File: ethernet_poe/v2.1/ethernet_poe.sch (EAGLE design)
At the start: 81 parts, among them J3 ARJM11C7-104-AB-EW2, U1 AZ1117EH-3.3TRG1, U2 IFX91041, U3 W5500, U4 TPS26600PWPR, X1 25MHz

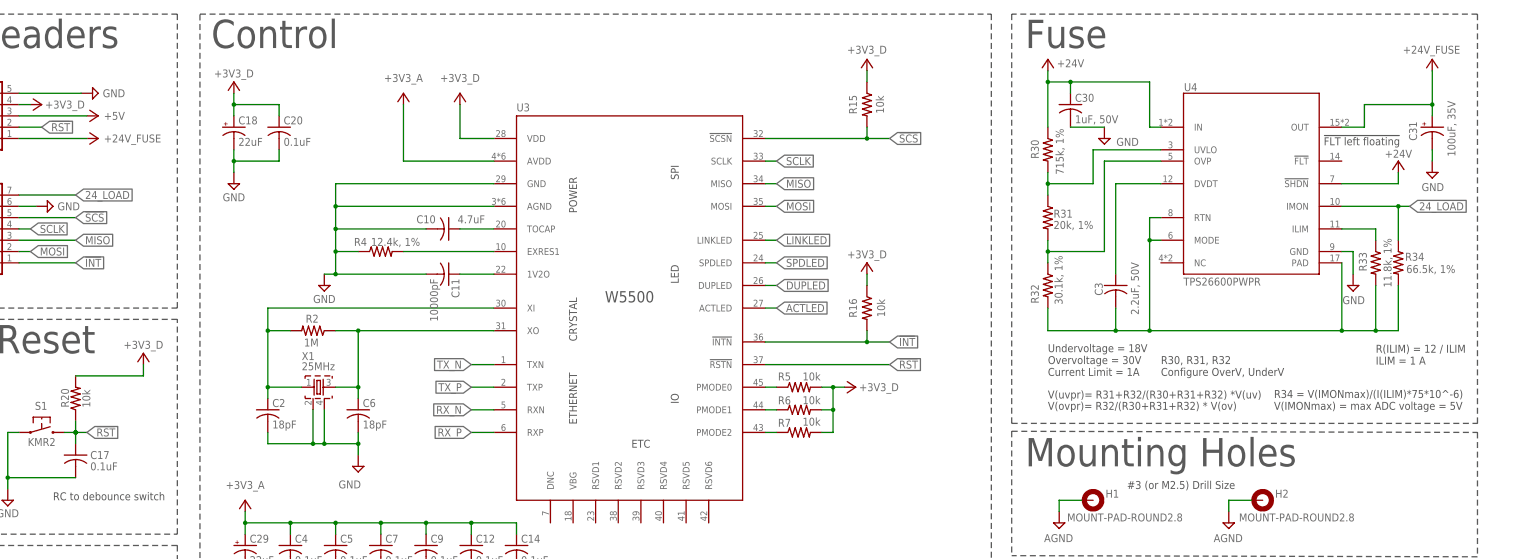
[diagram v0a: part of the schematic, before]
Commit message: Finished schematic and library changes
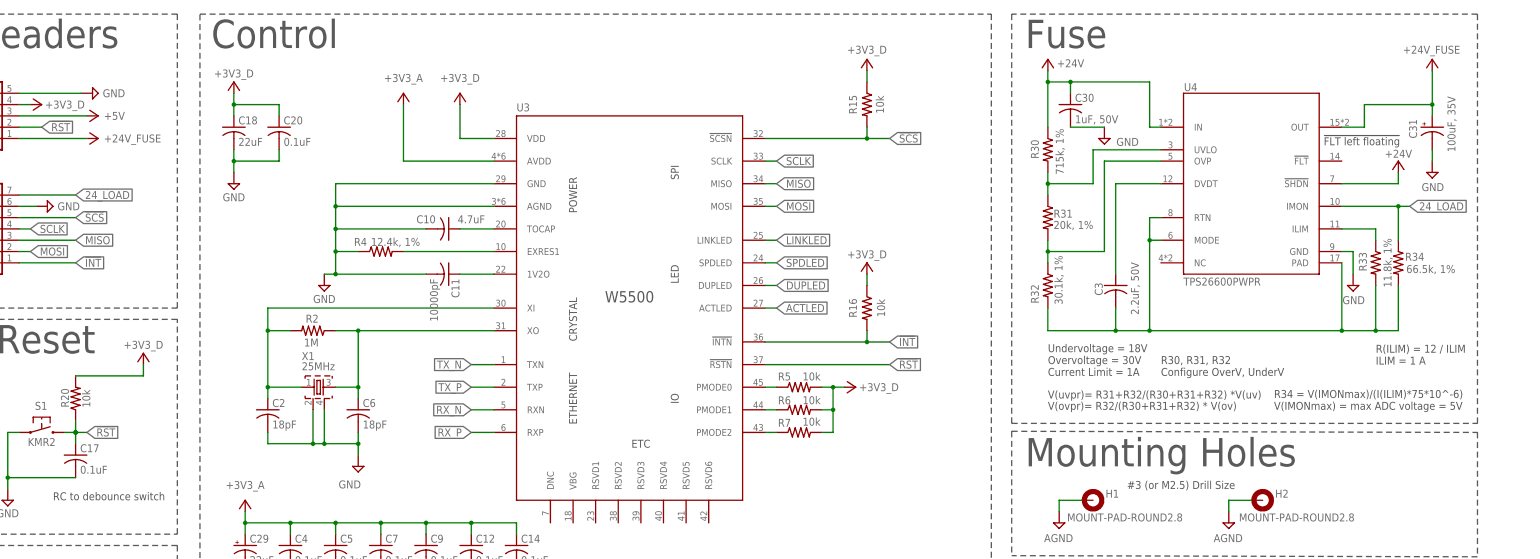
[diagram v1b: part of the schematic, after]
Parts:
- C15: DKPN (none) -> 732-8598-1-ND
- C17, C20, C21: device rcl:C-USC0603 -> adafruit:C-USC0402
- C18: device rcl:CPOL-USE2-5 -> rcl:C-USC0603
- C31: device rcl:CPOL-USE2-5 -> rcl:CPOL-USE2.5-7; DKPN (none) -> 732-8942-1-ND
- X1: device ethernet_poe:ABM10-25.000MHZ-18-E30-T3 -> ethernet_poe_v2.1:ABM10W-25.0000MHZ-6-K1Z-T3
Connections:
- net +3V3_D: now also C18.1; no longer C18.+
- net GND: now also C18.2; no longer C18.-

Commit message: Finished board changes
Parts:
- C1: value 22nF, 50V -> 0.022uF, 50V
- L1: device Wurth_Electronic_Inductors:WE-PD_7345_744777147 -> ethernet_poe_v2.1:7447709470_7447709470
- renumbered D8 to D4, L3 to L2, R29 to R28, R30 to R27, R31 to R14, R32 to R13, R33 to R12, R34 to R11, R35 to R9, R36 to R10
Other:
- note added: "L_out = ((V_in - V_out) * V_out)/ (I_rip * f_s * V_in) 42.7uF = ((24-5)*5)/(0.25*370000*24) I_sat > 3.5A"
